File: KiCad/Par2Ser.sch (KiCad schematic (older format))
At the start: 38 parts, among them J1 DB25_Male, J2 USB_C_Receptacle_USB2.0, J3 Conn_02x05_Odd_Even, U1 LC4032V-5TN48C, U2 FT240XS-R

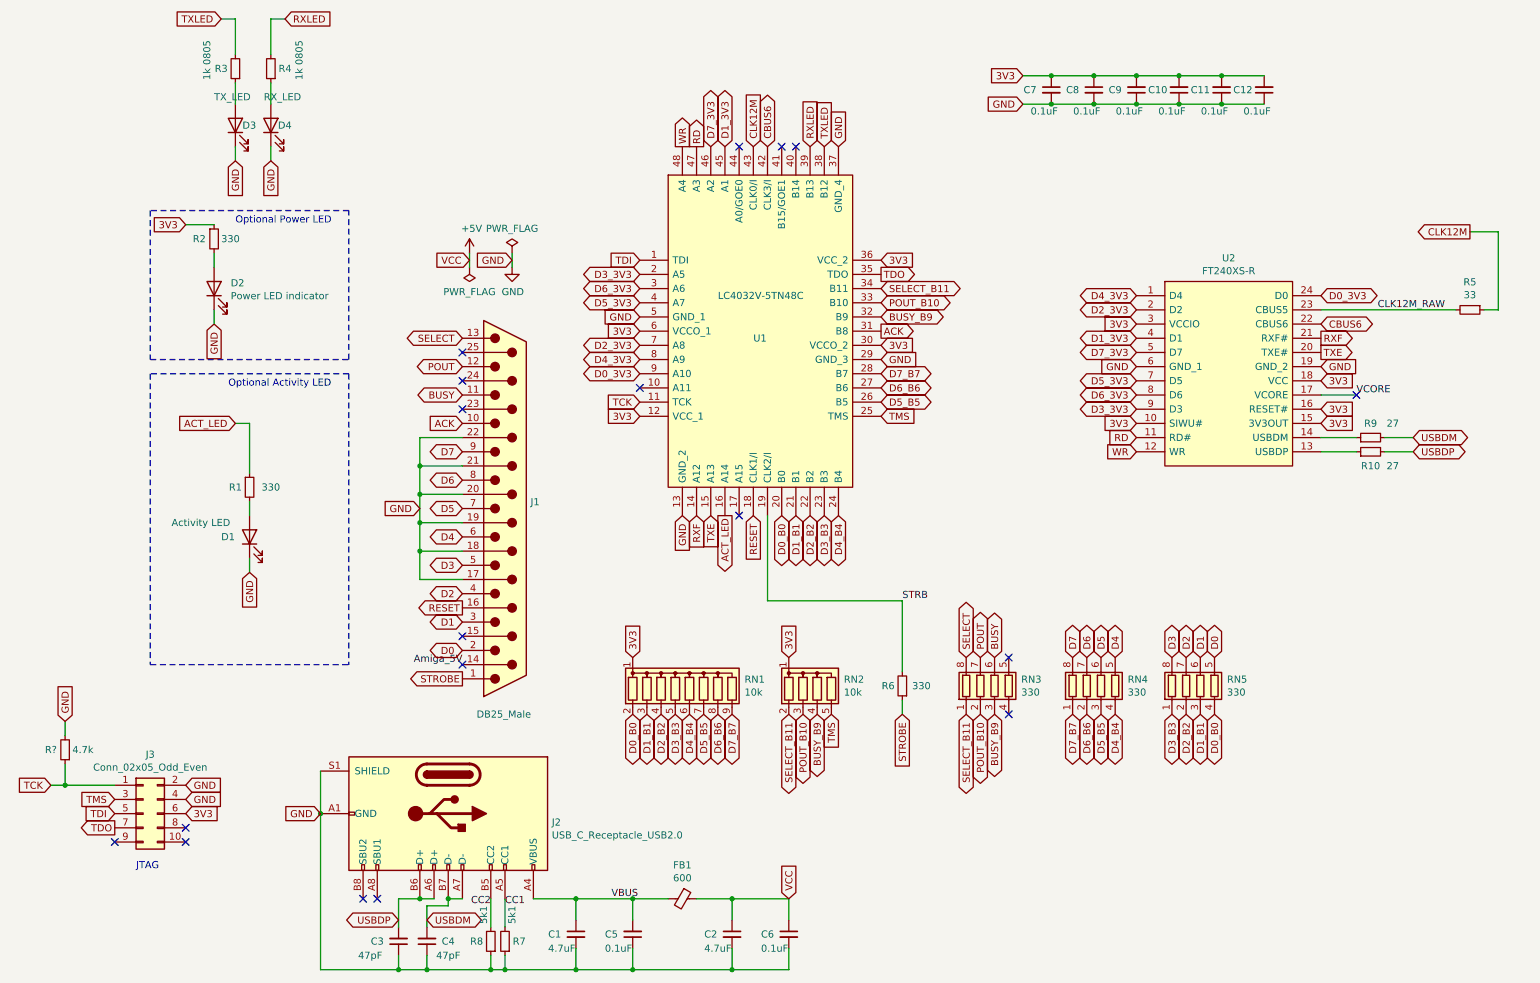
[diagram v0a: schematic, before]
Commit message: Add 3.3V regulator (TLV75533PDBVR) in SOT-23-5 package and add a 1 uF 0805 decoupling near VOUT pin and complete 3V3 routing and stitching
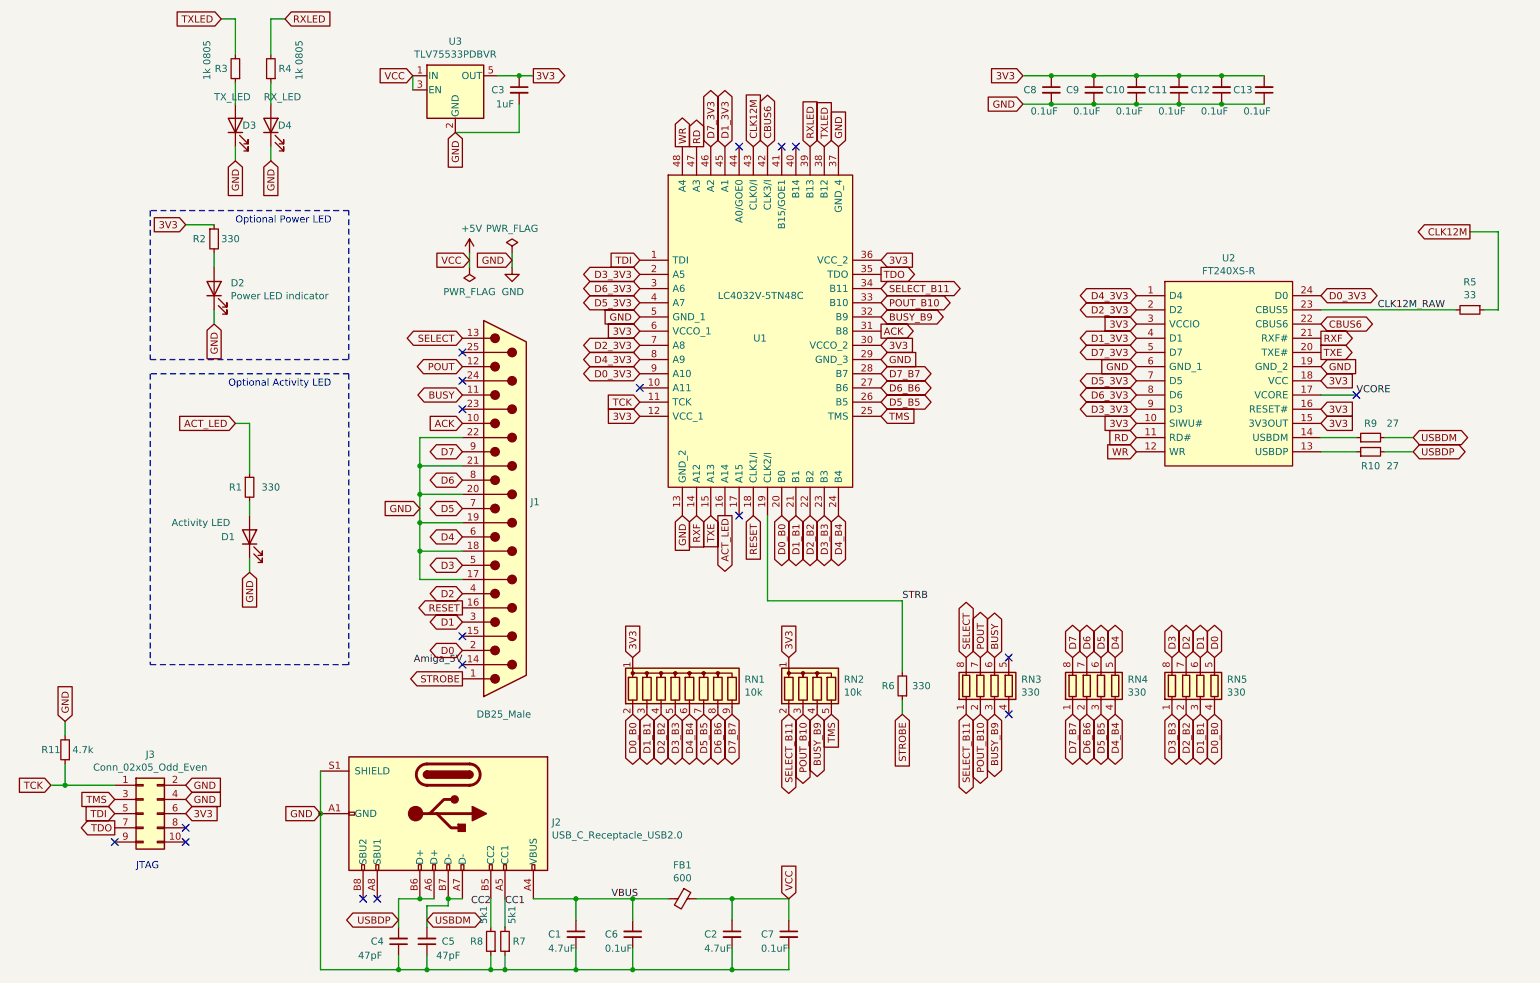
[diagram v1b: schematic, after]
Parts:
- added C3: 1uF, Capacitor_SMD:C_0805_2012Metric_Pad1.18x1.45mm_HandSolder, symbol Device:C_Small
- added U3: TLV75533PDBVR, Package_TO_SOT_SMD:SOT-23-5, symbol Regulator_Linear:TLV73312PDBV
- gave numbers to parts that had none: 1
- renumbered C9 to C10, C10 to C11, C11 to C12, C12 to C13, C3 to C4, C4 to C5, C5 to C6, C6 to C7, C7 to C8, C8 to C9
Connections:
- net +5V: now also U3.1 (IN), U3.3 (EN)
- net 3V3: now also C3.1, U3.5 (OUT)
- net GND: now also C3.2, U3.2 (GND)
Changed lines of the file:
@@
 $EndComp
 $Comp
-L Device:C_Small C9
+L Device:C_Small C10
 U 1 1 611D1D5F
 P 8500 1250
-F 0 "C9" H 8650 1250 50  0000 C CNN
+F 0 "C10" H 8650 1250 50  0000 C CNN
 F 1 "0.1uF" H 8550 1400 50  0000 C CNN
 F 2 "Capacitor_SMD:C_0603_1608Metric_Pad1.08x0.95mm_HandSolder" H 8500 1250 50  0001 C CNN
@@
 $EndComp
 $Comp
-L Device:C_Small C7
+L Device:C_Small C8
 U 1 1 612089E2
 P 7900 1250
-F 0 "C7" H 7750 1250 50  0000 C CNN
+F 0 "C8" H 7750 1250 50  0000 C CNN
 F 1 "0.1uF" H 7850 1100 50  0000 C CNN
 F 2 "Capacitor_SMD:C_0805_2012Metric_Pad1.18x1.45mm_HandSolder" H 7900 1250 50  0001 C CNN
@@
 Amiga_5V
 $Comp
-L Device:C_Small C6
+L Device:C_Small C7
 U 1 1 67141D33
 P 6050 7200
-F 0 "C6" H 5900 7200 50  0000 C CNN
+F 0 "C7" H 5900 7200 50  0000 C CNN
 F 1 "0.1uF" H 5950 7100 50  0000 C CNN
 F 2 "Capacitor_SMD:C_0805_2012Metric_Pad1.18x1.45mm_HandSolder" H 6050 7200 50  0001 C CNN
@@
 GND
 $Comp
-L Device:C_Small C5
+L Device:C_Small C6
 U 1 1 67247829
 P 4950 7200
-F 0 "C5" H 5100 7200 50  0000 C CNN
+F 0 "C6" H 5100 7200 50  0000 C CNN
 F 1 "0.1uF" H 5050 7300 50  0000 C CNN
 F 2 "Capacitor_SMD:C_0805_2012Metric_Pad1.18x1.45mm_HandSolder" H 4950 7200 50  0001 C CNN
@@
 	3500 7450 3300 7450
 $Comp
-L Device:C_Small C3
+L Device:C_Small C4
 U 1 1 671F8752
 P 3300 7250
-F 0 "C3" H 3450 7250 50  0000 C CNN
+F 0 "C4" H 3450 7250 50  0000 C CNN
 F 1 "47pF" H 3500 7350 50  0000 C CNN
 F 2 "Capacitor_SMD:C_0603_1608Metric_Pad1.08x0.95mm_HandSolder" H 3300 7250 50  0001 C CNN
@@
 $EndComp
 $Comp
-L Device:C_Small C4
+L Device:C_Small C5
 U 1 1 671FEDD5
 P 3500 7250
-F 0 "C4" H 3350 7250 50  0000 C CNN
+F 0 "C5" H 3350 7250 50  0000 C CNN
 F 1 "47pF" H 3350 7350 50  0000 C CNN
 F 2 "Capacitor_SMD:C_0603_1608Metric_Pad1.08x0.95mm_HandSolder" H 3500 7250 50  0001 C CNN
@@
 STRB
 $Comp
-L Device:C_Small C8
+L Device:C_Small C9
 U 1 1 5EB53531
 P 8200 1250
-F 0 "C8" H 8050 1250 50  0000 C CNN
+F 0 "C9" H 8050 1250 50  0000 C CNN
 F 1 "0.1uF" H 8150 1100 50  0000 C CNN
 F 2 "Capacitor_SMD:C_0603_1608Metric_Pad1.08x0.95mm_HandSolder" H 8200 1250 50  0001 C CNN
@@
 	10450 3800 10250 3800
 $Comp
-L Device:C_Small C10
+L Device:C_Small C11
 U 1 1 6A632E26
 P 8800 1250
-F 0 "C10" H 8950 1250 50  0000 C CNN
+F 0 "C11" H 8950 1250 50  0000 C CNN
 F 1 "0.1uF" H 8850 1400 50  0000 C CNN
 F 2 "Capacitor_SMD:C_0603_1608Metric_Pad1.08x0.95mm_HandSolder" H 8800 1250 50  0001 C CNN
@@
 Connection ~ 8500 1350
 $Comp
-L Device:C_Small C11
+L Device:C_Small C12
 U 1 1 6A647103
 P 9100 1250
-F 0 "C11" H 9250 1250 50  0000 C CNN
+F 0 "C12" H 9250 1250 50  0000 C CNN
 F 1 "0.1uF" H 9150 1400 50  0000 C CNN
 F 2 "Capacitor_SMD:C_0603_1608Metric_Pad1.08x0.95mm_HandSolder" H 9100 1250 50  0001 C CNN
@@
 Connection ~ 8800 1350
 $Comp
-L Device:C_Small C12
+L Device:C_Small C13
 U 1 1 6A67B251
 P 9400 1250
-F 0 "C12" H 9550 1250 50  0000 C CNN
+F 0 "C13" H 9550 1250 50  0000 C CNN
 F 1 "0.1uF" H 9450 1400 50  0000 C CNN
 F 2 "Capacitor_SMD:C_0603_1608Metric_Pad1.08x0.95mm_HandSolder" H 9400 1250 50  0001 C CNN
@@
 JTAG
 $Comp
-L Device:R_Small R?
+L Device:R_Small R11
 U 1 1 6A16EF59
 P 950 5900
-F 0 "R?" H 1050 5900 50  0000 C CNN
+F 0 "R11" H 1050 5900 50  0000 C CNN
 F 1 "4.7k" H 750 5900 50  0000 L CNN
 F 2 "Resistor_SMD:R_0805_2012Metric_Pad1.20x1.40mm_HandSolder" H 950 5900 50  0001 C CNN
@@
 Wire Wire Line
 	950  6150 1300 6150
+$Comp
+L Regulator_Linear:TLV73312PDBV U3
+U 1 1 6A18516F
+P 3700 1250
+F 0 "U3" H 3700 1592 50  0000 C CNN
+F 1 "TLV75533PDBVR" H 3700 1501 50  0000 C CNN
+F 2 "Package_TO_SOT_SMD:SOT-23-5" H 3700 1575 50  0001 C CIN
+F 3 "" H 3700 1250 50  0001 C CNN
+	1    3700 1250
+	1    0    0    -1
+$EndComp
+Text GLabel 3700 1550 3    50   Input ~ 0
+GND
+Text GLabel 4250 1150 2    50   Output ~ 0
+3V3
+Text GLabel 3400 1150 0    50   Input ~ 0
+VCC
+Wire Wire Line
+	3400 1150 3400 1250
+$Comp
+L Device:C_Small C3
+U 1 1 6A19BC5B
+P 4150 1250
+F 0 "C3" H 4000 1250 50  0000 C CNN
+F 1 "1uF" H 4050 1150 50  0000 C CNN
+F 2 "Capacitor_SMD:C_0805_2012Metric_Pad1.18x1.45mm_HandSolder" H 4150 1250 50  0001 C CNN
+F 3 "~" H 4150 1250 50  0001 C CNN
+	1    4150 1250
+	1    0    0    -1
+$EndComp
+Wire Wire Line
+	4000 1150 4150 1150
+Connection ~ 4150 1150
+Wire Wire Line
+	4150 1150 4250 1150
+Wire Wire Line
+	3700 1550 4150 1550
+Wire Wire Line
+	4150 1550 4150 1350
 $EndSCHEMATC

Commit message: Add 32 Hz MEMS oscillator (SIT1534AI-H4-DCC-00.032) on clk3 input (pin 42)
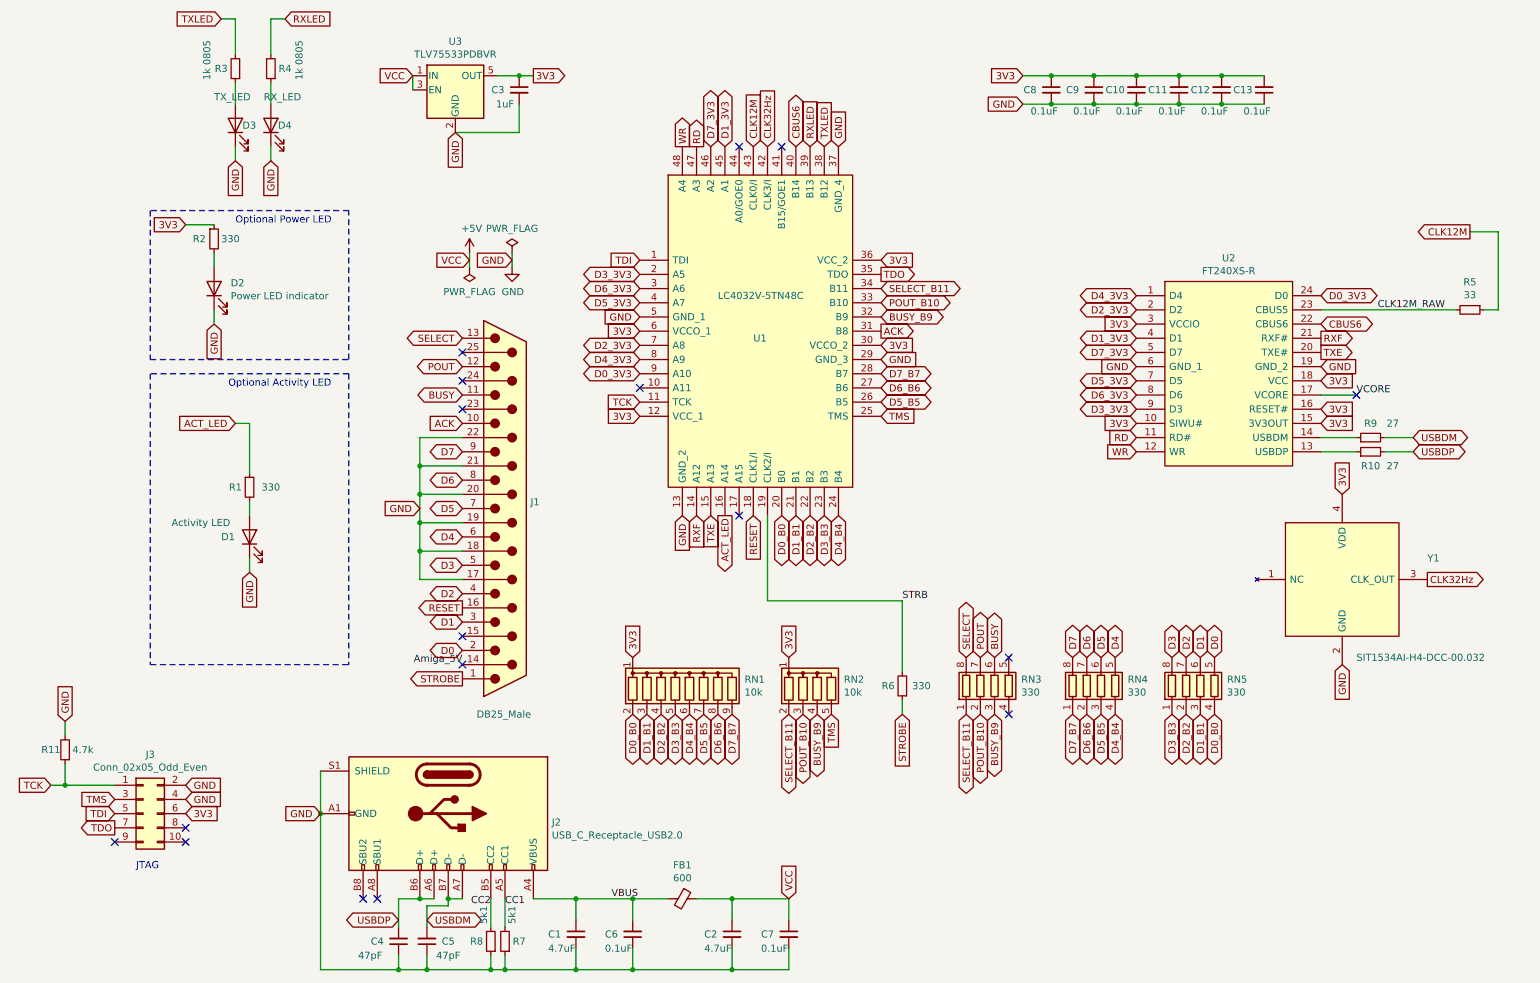
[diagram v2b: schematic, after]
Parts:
- added Y1: SIT1534AI-H4-DCC-00.032, Par2Ser:SIT1534AIH4DCC00256, symbol Par2Ser:SIT1534AI-H4-DCC-00.032
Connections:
- net 3V3: now also Y1.4 (VDD)
- net CBUS6: now also U1.40 (B14); no longer U1.42 (CLK3/I)
- net GND: now also Y1.2 (GND)
- new net CLK32Hz: U1.42 (CLK3/I), Y1.3 (CLK_OUT)
- no-connect marks 18 -> 17
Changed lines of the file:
@@
 Text GLabel 10850 2250 0    50   Output ~ 0
 CLK12M
-Text GLabel 5900 1650 1    50   BiDi ~ 0
+Text GLabel 6100 1650 1    50   BiDi ~ 0
 CBUS6
 Text GLabel 9800 2900 2    50   BiDi ~ 0
@@
 NoConn ~ 5000 3350
 NoConn ~ 6000 1650
-NoConn ~ 6100 1650
 NoConn ~ 5700 4250
 $Comp
@@
 Wire Wire Line
 	4150 1550 4150 1350
+Text GLabel 5900 1650 1    50   Input ~ 0
+CLK32Hz
+Text GLabel 9950 5300 3    50   Input ~ 0
+GND
+Text GLabel 9950 4100 1    50   Input ~ 0
+3V3
+Text GLabel 10550 4700 2    50   Output ~ 0
+CLK32Hz
+$Comp
+L Par2Ser:SIT1534AI-H4-DCC-00.032 Y1
+U 1 1 6A21EC58
+P 9950 4700
+F 0 "Y1" H 10550 4850 50  0000 L CNN
+F 1 "SIT1534AI-H4-DCC-00.032" H 10050 4150 50  0000 L CNN
+F 2 "Par2Ser:SIT1534AIH4DCC00256" H 10400 5100 50  0001 L CNN
+F 3 "https://www.sitime.com/support/resource-library/datasheets/sit1534-datasheet" H 10400 5000 50  0001 L CNN
+	1    9950 4700
+	1    0    0    -1
+$EndComp
 $EndSCHEMATC
